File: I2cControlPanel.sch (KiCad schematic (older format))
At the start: 54 parts, among them J1 JoystickL, J2 Conn_01x06, J3 Conn_01x04, J4 Conn_01x04, J5 JoystickR, J6 Conn_01x04, SW6 SW_Push, U1 NJM12888F33, U2 ATmega328PB-MU, U3 AQM0802

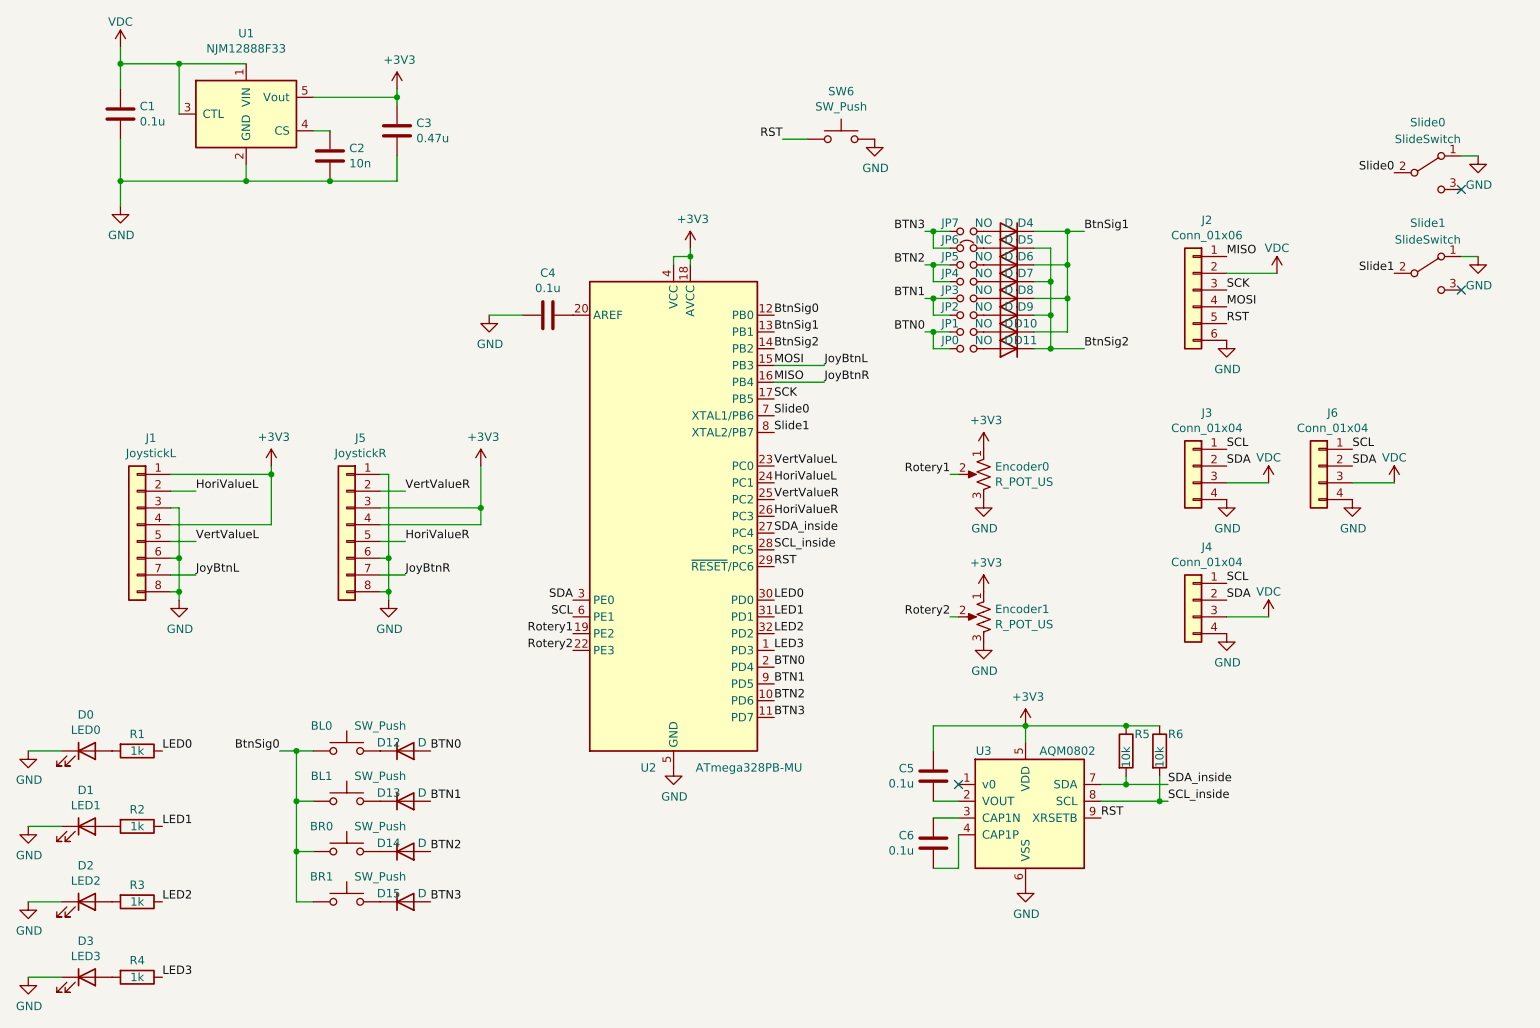
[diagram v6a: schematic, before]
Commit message: Use diode array and add mounting holes as Rev2021.03
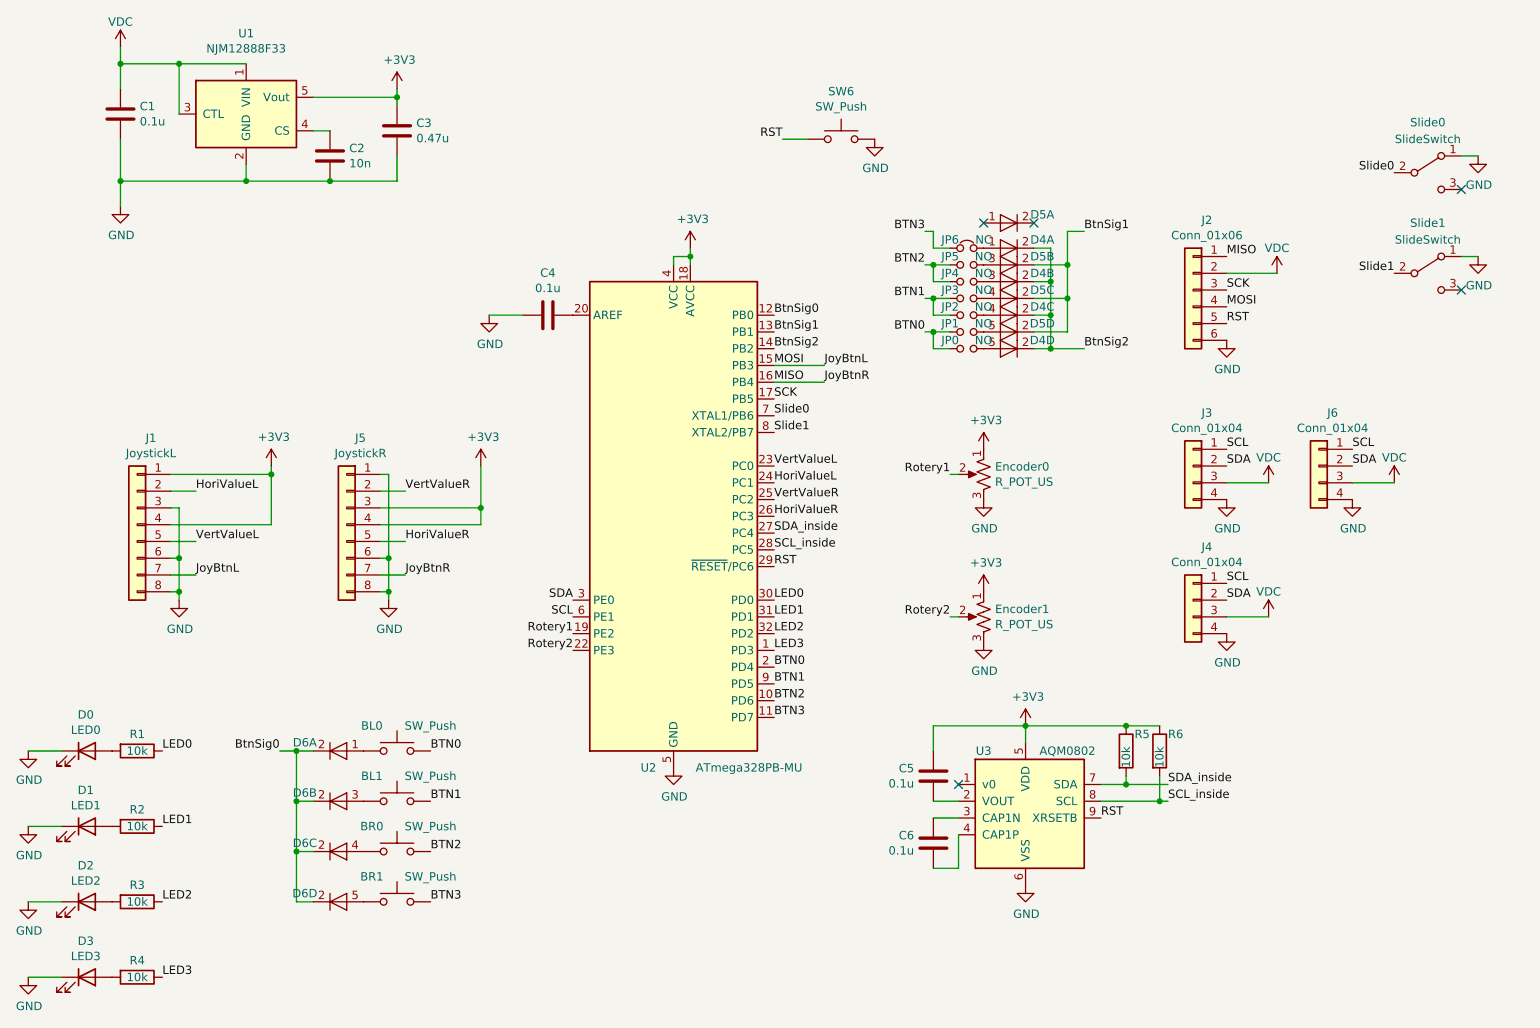
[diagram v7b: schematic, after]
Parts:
- removed D10, D11, D12, D13, D14, D15, D4, D5, D6, D7, D8, D9: D, my-kicad-footprints:D_SOD-523F, symbol Device:D
- removed JP7: NO, Jumper:SolderJumper-2_P1.3mm_Open_RoundedPad1.0x1.5mm, symbol I2cControlPanel-rescue:Jumper_NO_Small-Device
- added D4, D5, D6: 1SS309, my-kicad-footprints:SC-74-5_1.6x2.9mm_P0.95mm, symbol my-kicad-symbols:Diode_4array_1SS309
- R1, R2, R3, R4: value 1k -> 10k
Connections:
- net BTN0: now also BL0.2
- net BTN1: now also BL1.2
- net BTN2: now also BR0.2
- net BTN3: now also BR1.2
- net BtnSig0: now also D6.2, D6.2, D6.2, D6.2; no longer BL0.1, BL1.1, BR0.1, BR1.1
- net BtnSig1: now also D5.2, D5.2, D5.2
- net BtnSig2: now also D4.2, D4.2, D4.2, D4.2
- net at JP6.2: now also D4.1
- net at JP2.2: now also D4.4
- net at JP5.2: now also D5.3
- net at JP4.2: now also D4.3
- net at JP3.2: now also D5.4
- net at JP1.2: now also D5.5
- net at JP0.2: now also D4.5
- new net: BL0.1, D6.1
- new net: BL1.1, D6.3
- new net: BR0.1, D6.4
- new net: BR1.1, D6.5
- no-connect marks 3 -> 5
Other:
- moved on the sheet: BL0, BL1, BR0, BR1

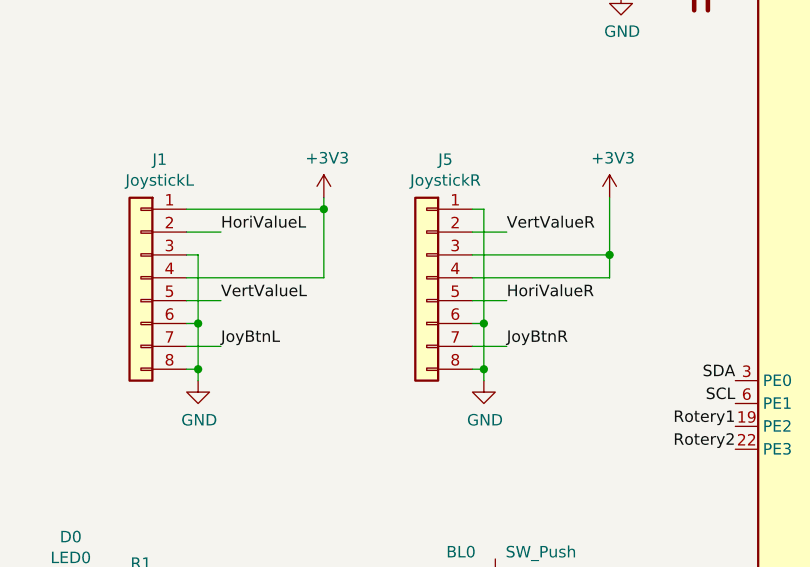
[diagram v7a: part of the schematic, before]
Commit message: Change joystick for ps4 type
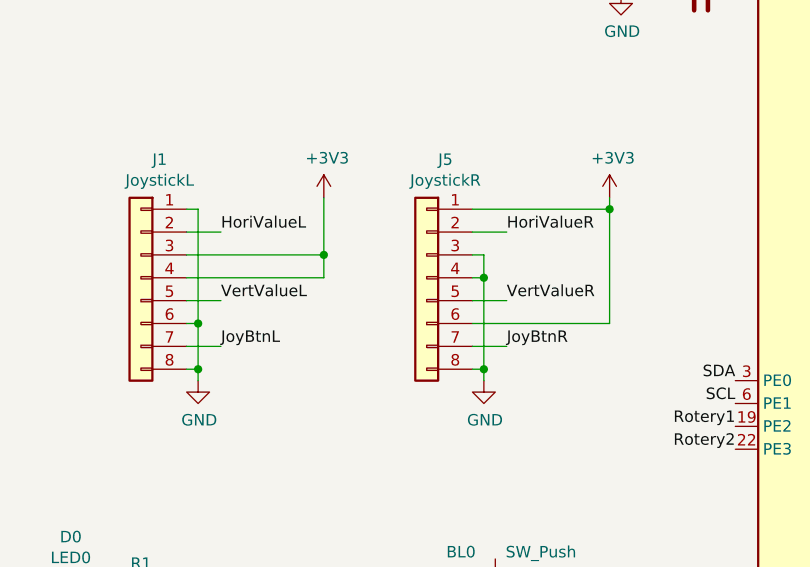
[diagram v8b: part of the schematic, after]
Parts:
- J1, J5: footprint my-kicad-footprints:LowHeightJoyStickWithButton -> my-kicad-footprints:PS4tJoystick
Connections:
- net +3V3: now also J1.3 (Pin_3), J5.1 (Pin_1), J5.6 (Pin_6); no longer J1.1 (Pin_1), J5.3 (Pin_3), J5.4 (Pin_4)
- net GND: now also J1.1 (Pin_1), J5.3 (Pin_3), J5.4 (Pin_4); no longer J1.3 (Pin_3), J5.1 (Pin_1), J5.6 (Pin_6)
- net HoriValueR: now also J5.2 (Pin_2); no longer J5.5 (Pin_5)
- net VertValueR: now also J5.5 (Pin_5); no longer J5.2 (Pin_2)
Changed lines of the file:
@@
 HoriValueL
-Wire Wire Line
-	3450 3500 3450 3550
-Connection ~ 3450 3550
-Wire Wire Line
-	3450 3550 3450 3850
 Wire Wire Line
 	3000 3650 2850 3650
@@
 $EndComp
 Wire Wire Line
-	2850 3550 3450 3550
-Wire Wire Line
 	2850 3850 3450 3850
-Wire Wire Line
-	2850 3750 2900 3750
-Wire Wire Line
-	2900 3750 2900 4050
 Connection ~ 2900 4050
 $Comp
@@
 	1    0    0    -1
 $EndComp
+Text Label 4250 3950 0    50   ~ 0
+VertValueR
 Text Label 4250 3650 0    50   ~ 0
-VertValueR
-Text Label 4250 3950 0    50   ~ 0
 HoriValueR
 Wire Wire Line
@@
 F 0 "J1" H 2568 4367 50  0000 C CNN
 F 1 "JoystickL" H 2568 4276 50  0000 C CNN
-F 2 "my-kicad-footprints:LowHeightJoyStickWithButton" H 2650 3850 50  0001 C CNN
+F 2 "my-kicad-footprints:PS4tJoystick" H 2650 3850 50  0001 C CNN
 F 3 "~" H 2650 3850 50  0001 C CNN
 	1    2650 3850
@@
 F 0 "J5" H 3818 4367 50  0000 C CNN
 F 1 "JoystickR" H 3818 4276 50  0000 C CNN
-F 2 "my-kicad-footprints:LowHeightJoyStickWithButton" H 3900 3850 50  0001 C CNN
+F 2 "my-kicad-footprints:PS4tJoystick" H 3900 3850 50  0001 C CNN
 F 3 "~" H 3900 3850 50  0001 C CNN
 	1    3900 3850
@@
 	10550 2250 10650 2250
 Wire Wire Line
-	4100 3850 4700 3850
-Wire Wire Line
-	4100 3750 4700 3750
-Connection ~ 4700 3750
-Wire Wire Line
-	4700 3750 4700 3850
-Wire Wire Line
-	4700 3500 4700 3750
-Wire Wire Line
-	4100 3550 4150 3550
-Wire Wire Line
-	4150 3550 4150 4050
-Connection ~ 4150 4250
-Wire Wire Line
-	4150 4050 4100 4050
-Connection ~ 4150 4050
-Wire Wire Line
-	4150 4050 4150 4250
-Wire Wire Line
 	6500 1550 6650 1550
 $Comp
@@
 	1    0    0    -1
 $EndComp
+Wire Wire Line
+	3450 3500 3450 3750
+Wire Wire Line
+	2900 3550 2850 3550
+Wire Wire Line
+	2900 3550 2900 4050
+Wire Wire Line
+	2850 3750 3450 3750
+Connection ~ 3450 3750
+Wire Wire Line
+	3450 3750 3450 3850
+Wire Wire Line
+	4100 4050 4700 4050
+Wire Wire Line
+	4700 3500 4700 3550
+Wire Wire Line
+	4100 3550 4700 3550
+Connection ~ 4700 3550
+Wire Wire Line
+	4700 3550 4700 4050
+Wire Wire Line
+	4100 3750 4150 3750
+Wire Wire Line
+	4150 3750 4150 3850
+Connection ~ 4150 4250
+Wire Wire Line
+	4150 3850 4100 3850
+Connection ~ 4150 3850
+Wire Wire Line
+	4150 3850 4150 4250
 $EndSCHEMATC
